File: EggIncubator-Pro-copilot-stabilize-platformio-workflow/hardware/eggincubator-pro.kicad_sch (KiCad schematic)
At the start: 36 parts, among them J1 ESP32 DevKit breakout, J10 ESP32 DevKit 5V / VIN input, J11 BTS7960 motor supply input, J2 SHT31 module, I2C 0x44, J3 DS18B20, 1-Wire, J4 4 optocoupled relay-control o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, J5 BTS7960 module / motor (separ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, J6 Door and turner limit switches, J7 5V buzzer module, Q1 low-side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, J8 Expansion: I2C / ADC sensors, J9 12V DC input, Q1 PN2222A, U1 PC817, U2 PC817, U3 PC817, U4 PC817, U9 12V to 5V buck module

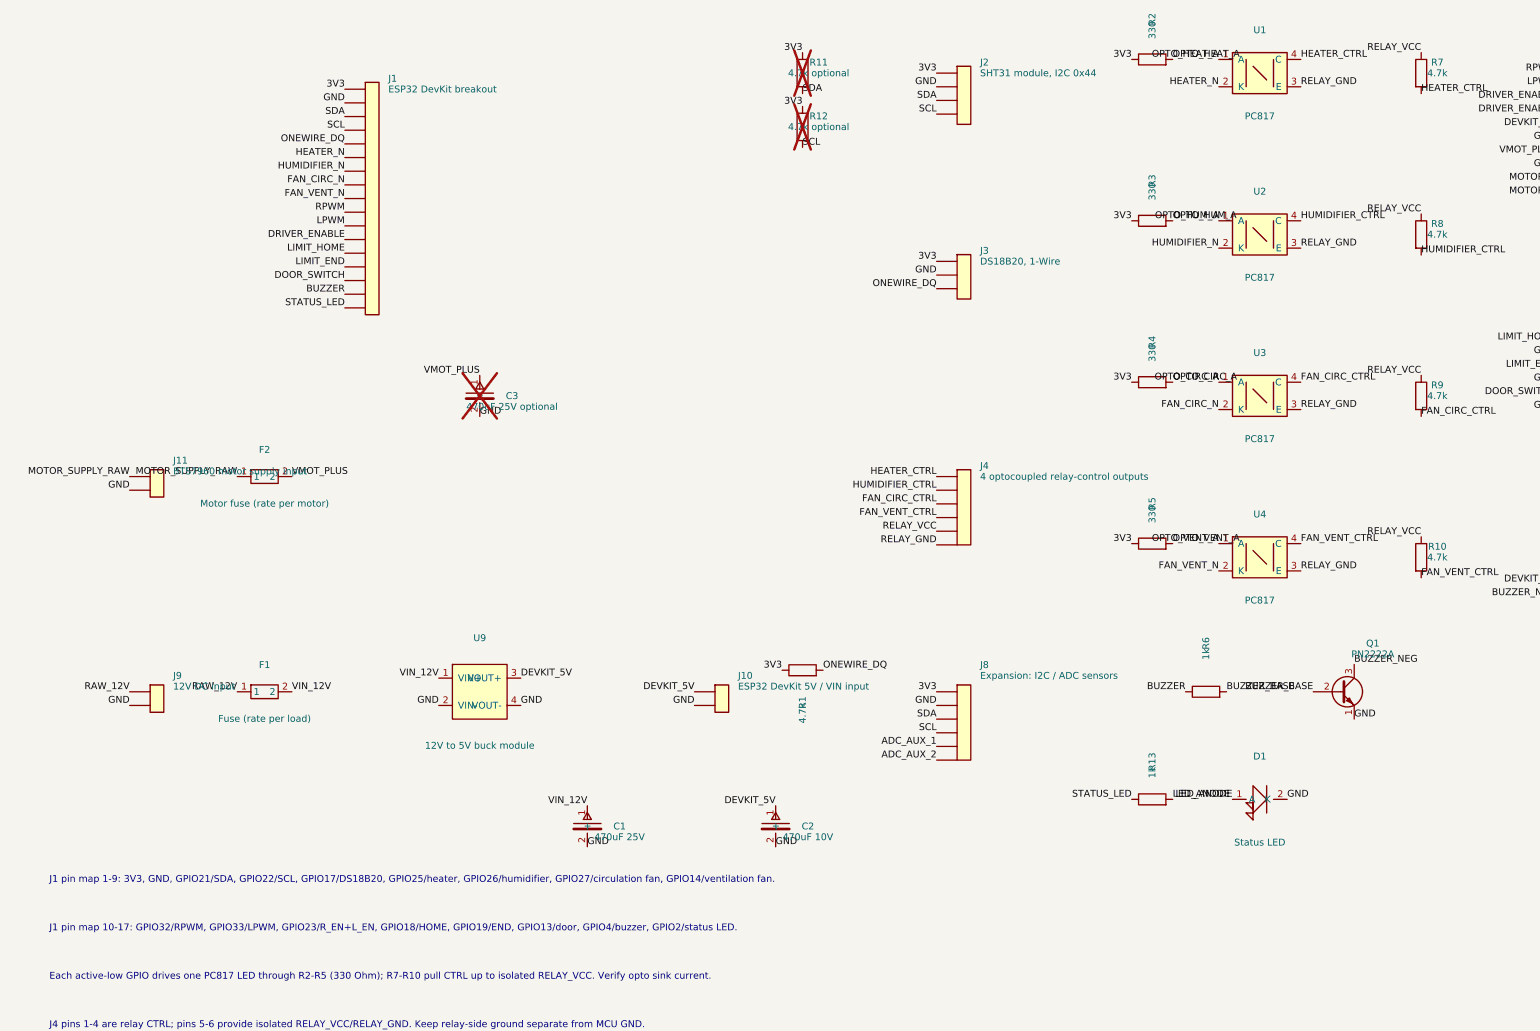
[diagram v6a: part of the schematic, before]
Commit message: Show ESP32 DevKit in KiCad schematic
Co-authored-by: tomnyle <175001228+tomnyle@users.noreply.github.com>
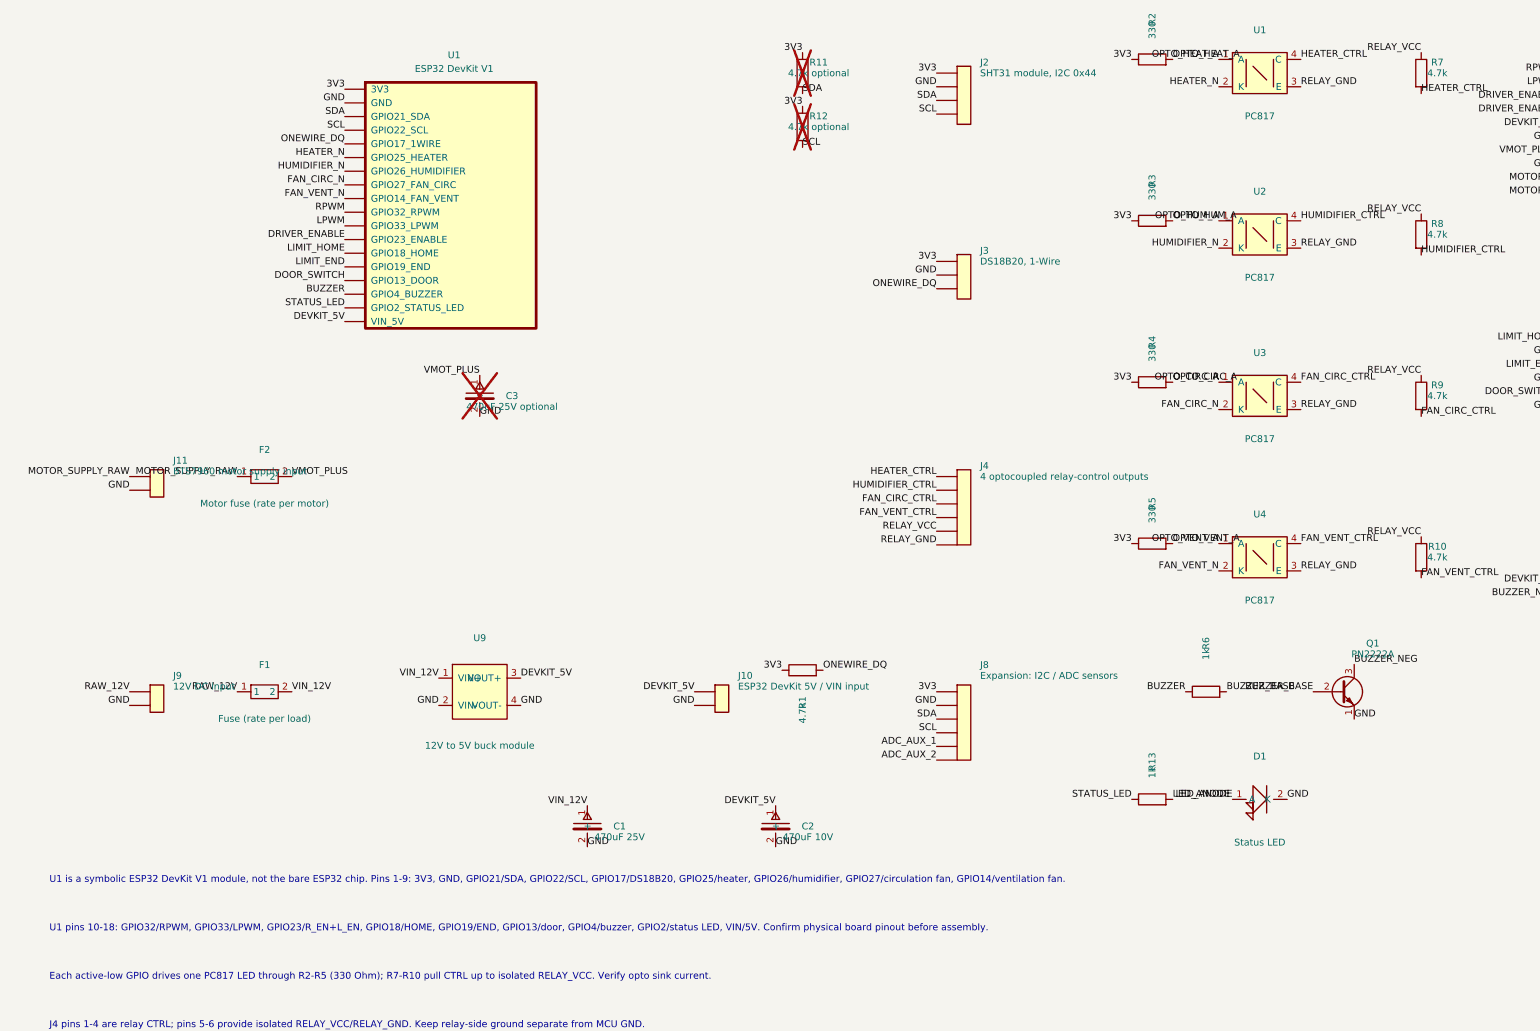
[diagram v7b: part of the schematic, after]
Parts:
- removed J1: ESP32 DevKit breakout, symbol Connector_Generic:Conn_01x17
- added U1: ESP32 DevKit V1, symbol EggIncubator:ESP32_DevKit_V1
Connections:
- net 3V3: now also U1.1 (3V3)
- net BUZZER: now also U1.16 (GPIO4_BUZZER)
- net DEVKIT_5V: now also U1.18 (VIN_5V)
- net DOOR_SWITCH: now also U1.15 (GPIO13_DOOR)
- net DRIVER_ENABLE: now also U1.12 (GPIO23_ENABLE)
- net FAN_CIRC_N: now also U1.8 (GPIO27_FAN_CIRC)
- net FAN_VENT_N: now also U1.9 (GPIO14_FAN_VENT)
- net GND: now also U1.2 (GND)
- net HEATER_N: now also U1.6 (GPIO25_HEATER)
- net HUMIDIFIER_N: now also U1.7 (GPIO26_HUMIDIFIER)
- net LIMIT_END: now also U1.14 (GPIO19_END)
- net LIMIT_HOME: now also U1.13 (GPIO18_HOME)
- net LPWM: now also U1.11 (GPIO33_LPWM)
- net ONEWIRE_DQ: now also U1.5 (GPIO17_1WIRE)
- net RPWM: now also U1.10 (GPIO32_RPWM)
- net SCL: now also U1.4 (GPIO22_SCL)
- net SDA: now also U1.3 (GPIO21_SDA)
- net STATUS_LED: now also U1.17 (GPIO2_STATUS_LED)
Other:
- note added: "U1 is a symbolic ESP32 DevKit V1 module, not the bare ESP32 chip. Pins 1-9: 3V3, GND, GPIO21/SDA, GPIO22/SCL, GPIO17/DS18B20, GPIO25/heater, GPIO26/humidifier, GPIO27/circulation fan, GPIO14/ventilation fan."
- note added: "U1 pins 10-18: GPIO32/RPWM, GPIO33/LPWM, GPIO23/R_EN+L_EN, GPIO18/HOME, GPIO19/END, GPIO13/door, GPIO4/buzzer, GPIO2/status LED, VIN/5V. Confirm physical board pinout before assembly."
- note removed: "J1 pin map 1-9: 3V3, GND, GPIO21/SDA, GPIO22/SCL, GPIO17/DS18B20, GPIO25/heater, GPIO26/humidifier, GPIO27/circulation fan, GPIO14/ventilation fan."
- note removed: "J1 pin map 10-17: GPIO32/RPWM, GPIO33/LPWM, GPIO23/R_EN+L_EN, GPIO18/HOME, GPIO19/END, GPIO13/door, GPIO4/buzzer, GPIO2/status LED."
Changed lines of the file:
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@@
     (comment 2 "Not a mains wiring or PCB fabrication drawing.")
   )
-  (symbol (lib_id "Connector_Generic:Conn_01x17") (at 105 58 0) (unit 1) (in_bom yes) (on_board yes) (dnp no)
-    (property "Reference" "J1" (at 108 56 0) (effects (font (size 1.27 1.27)) (justify left)))
-    (property "Value" "ESP32 DevKit breakout" (at 108 58 0) (effects (font (size 1.27 1.27)) (justify left)))
+  (symbol (lib_id "EggIncubator:ESP32_DevKit_V1") (at 105 58 0) (unit 1) (in_bom yes) (on_board yes) (dnp no)
+    (property "Reference" "U1" (at 120.24 51.65 0) (effects (font (size 1.27 1.27)) (justify center)))
+    (property "Value" "ESP32 DevKit V1" (at 120.24 54.19 0) (effects (font (size 1.27 1.27)) (justify center)))
     (property "Footprint" "" (at 105 58 0) (effects (font (size 1.27 1.27)) hide))
     (property "Datasheet" "~" (at 105 58 0) (effects (font (size 1.27 1.27)) hide))
-    (pin "1") (pin "2") (pin "3") (pin "4") (pin "5") (pin "6") (pin "7") (pin "8") (pin "9") (pin "10") (pin "11") (pin "12") (pin "13") (pin "14") (pin "15") (pin "16") (pin "17")
-    (instances (project "EggIncubator-Pro" (path "/60845d38-2cd0-4dd2-9a8c-c6c7c694e4e9/a165544d-56cd-43db-9b9d-925791539cc0" (reference "J1") (unit 1))))
+    (pin "1")
+    (pin "2")
+    (pin "3")
+    (pin "4")
+    (pin "5")
+    (pin "6")
+    (pin "7")
+    (pin "8")
+    (pin "9")
+    (pin "10")
+    (pin "11")
+    (pin "12")
+    (pin "13")
+    (pin "14")
+    (pin "15")
+    (pin "16")
+    (pin "17")
+    (pin "18")
+    (instances (project "EggIncubator-Pro" (path "/60845d38-2cd0-4dd2-9a8c-c6c7c694e4e9/00000000-0000-4000-8000-000000000173" (reference "U1") (unit 1))))
   )
   (symbol (lib_id "Connector_Generic:Conn_01x04") (at 215 55 0) (unit 1) (in_bom yes) (on_board yes) (dnp no)
@@
   (label "BUZZER" (at 99.92 96.10 180) (fields_autoplaced) (effects (font (size 1.27 1.27)) (justify right bottom)))
   (label "STATUS_LED" (at 99.92 98.64 180) (fields_autoplaced) (effects (font (size 1.27 1.27)) (justify right bottom)))
+  (label "DEVKIT_5V" (at 99.92 101.18 180) (fields_autoplaced) (effects (font (size 1.27 1.27)) (justify right bottom)))
   (label "3V3" (at 209.92 55 180) (fields_autoplaced) (effects (font (size 1.27 1.27)) (justify right bottom)))
   (label "GND" (at 209.92 57.54 180) (fields_autoplaced) (effects (font (size 1.27 1.27)) (justify right bottom)))
@@
   (label "VMOT_PLUS" (at 125 111.19 180) (fields_autoplaced) (effects (font (size 1.27 1.27)) (justify right bottom)))
   (label "GND" (at 125 118.81 0) (fields_autoplaced) (effects (font (size 1.27 1.27)) (justify left bottom)))
-  (text "J1 pin map 1-9: 3V3, GND, GPIO21/SDA, GPIO22/SCL, GPIO17/DS18B20, GPIO25/heater, GPIO26/humidifier, GPIO27/circulation fan, GPIO14/ventilation fan." (at 45 205 0) (effects (font (size 1.27 1.27)) (justify left)))
-  (text "J1 pin map 10-17: GPIO32/RPWM, GPIO33/LPWM, GPIO23/R_EN+L_EN, GPIO18/HOME, GPIO19/END, GPIO13/door, GPIO4/buzzer, GPIO2/status LED." (at 45 214 0) (effects (font (size 1.27 1.27)) (justify left)))
+  (text "U1 is a symbolic ESP32 DevKit V1 module, not the bare ESP32 chip. Pins 1-9: 3V3, GND, GPIO21/SDA, GPIO22/SCL, GPIO17/DS18B20, GPIO25/heater, GPIO26/humidifier, GPIO27/circulation fan, GPIO14/ventilation fan." (at 45 205 0) (effects (font (size 1.27 1.27)) (justify left)))
+  (text "U1 pins 10-18: GPIO32/RPWM, GPIO33/LPWM, GPIO23/R_EN+L_EN, GPIO18/HOME, GPIO19/END, GPIO13/door, GPIO4/buzzer, GPIO2/status LED, VIN/5V. Confirm physical board pinout before assembly." (at 45 214 0) (effects (font (size 1.27 1.27)) (justify left)))
   (text "Each active-low GPIO drives one PC817 LED through R2-R5 (330 Ohm); R7-R10 pull CTRL up to isolated RELAY_VCC. Verify opto sink current." (at 45 223 0) (effects (font (size 1.27 1.27)) (justify left)))
   (text "J4 pins 1-4 are relay CTRL; pins 5-6 provide isolated RELAY_VCC/RELAY_GND. Keep relay-side ground separate from MCU GND." (at 45 232 0) (effects (font (size 1.27 1.27)) (justify left)))

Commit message: Fix ESP32 reference and relay supply notes
Co-authored-by: tomnyle <175001228+tomnyle@users.noreply.github.com>
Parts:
- renumbered U1 to U5
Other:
- note added: "U5 is a symbolic ESP32 DevKit V1 module, not the bare ESP32 chip. Pins 1-9: 3V3, GND, GPIO21/SDA, GPIO22/SCL, GPIO17/DS18B20, GPIO25/heater, GPIO26/humidifier, GPIO27/circulation fan, GPIO14/ventilation fan."
- note added: "U5 pins 10-18: GPIO32/RPWM, GPIO33/LPWM, GPIO23/R_EN+L_EN, GPIO18/HOME, GPIO19/END, GPIO13/door, GPIO4/buzzer, GPIO2/status LED, VIN/5V. Confirm physical board pinout before assembly."
- note removed: "U1 is a symbolic ESP32 DevKit V1 module, not the bare ESP32 chip. Pins 1-9: 3V3, GND, GPIO21/SDA, GPIO22/SCL, GPIO17/DS18B20, GPIO25/heater, GPIO26/humidifier, GPIO27/circulation fan, GPIO14/ventilation fan."
- note removed: "U1 pins 10-18: GPIO32/RPWM, GPIO33/LPWM, GPIO23/R_EN+L_EN, GPIO18/HOME, GPIO19/END, GPIO13/door, GPIO4/buzzer, GPIO2/status LED, VIN/5V. Confirm physical board pinout before assembly."
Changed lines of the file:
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@@
   )
   (symbol (lib_id "EggIncubator:ESP32_DevKit_V1") (at 105 58 0) (unit 1) (in_bom yes) (on_board yes) (dnp no)
-    (property "Reference" "U1" (at 120.24 51.65 0) (effects (font (size 1.27 1.27)) (justify center)))
+    (property "Reference" "U5" (at 120.24 51.65 0) (effects (font (size 1.27 1.27)) (justify center)))
     (property "Value" "ESP32 DevKit V1" (at 120.24 54.19 0) (effects (font (size 1.27 1.27)) (justify center)))
     (property "Footprint" "" (at 105 58 0) (effects (font (size 1.27 1.27)) hide))
@@
     (pin "17")
     (pin "18")
-    (instances (project "EggIncubator-Pro" (path "/60845d38-2cd0-4dd2-9a8c-c6c7c694e4e9/00000000-0000-4000-8000-000000000173" (reference "U1") (unit 1))))
+    (instances (project "EggIncubator-Pro" (path "/60845d38-2cd0-4dd2-9a8c-c6c7c694e4e9/00000000-0000-4000-8000-000000000173" (reference "U5") (unit 1))))
   )
   (symbol (lib_id "Connector_Generic:Conn_01x04") (at 215 55 0) (unit 1) (in_bom yes) (on_board yes) (dnp no)
@@
   (label "VMOT_PLUS" (at 125 111.19 180) (fields_autoplaced) (effects (font (size 1.27 1.27)) (justify right bottom)))
   (label "GND" (at 125 118.81 0) (fields_autoplaced) (effects (font (size 1.27 1.27)) (justify left bottom)))
-  (text "U1 is a symbolic ESP32 DevKit V1 module, not the bare ESP32 chip. Pins 1-9: 3V3, GND, GPIO21/SDA, GPIO22/SCL, GPIO17/DS18B20, GPIO25/heater, GPIO26/humidifier, GPIO27/circulation fan, GPIO14/ventilation fan." (at 45 205 0) (effects (font (size 1.27 1.27)) (justify left)))
-  (text "U1 pins 10-18: GPIO32/RPWM, GPIO33/LPWM, GPIO23/R_EN+L_EN, GPIO18/HOME, GPIO19/END, GPIO13/door, GPIO4/buzzer, GPIO2/status LED, VIN/5V. Confirm physical board pinout before assembly." (at 45 214 0) (effects (font (size 1.27 1.27)) (justify left)))
+  (text "U5 is a symbolic ESP32 DevKit V1 module, not the bare ESP32 chip. Pins 1-9: 3V3, GND, GPIO21/SDA, GPIO22/SCL, GPIO17/DS18B20, GPIO25/heater, GPIO26/humidifier, GPIO27/circulation fan, GPIO14/ventilation fan." (at 45 205 0) (effects (font (size 1.27 1.27)) (justify left)))
+  (text "U5 pins 10-18: GPIO32/RPWM, GPIO33/LPWM, GPIO23/R_EN+L_EN, GPIO18/HOME, GPIO19/END, GPIO13/door, GPIO4/buzzer, GPIO2/status LED, VIN/5V. Confirm physical board pinout before assembly." (at 45 214 0) (effects (font (size 1.27 1.27)) (justify left)))
   (text "Each active-low GPIO drives one PC817 LED through R2-R5 (330 Ohm); R7-R10 pull CTRL up to isolated RELAY_VCC. Verify opto sink current." (at 45 223 0) (effects (font (size 1.27 1.27)) (justify left)))
   (text "J4 pins 1-4 are relay CTRL; pins 5-6 provide isolated RELAY_VCC/RELAY_GND. Keep relay-side ground separate from MCU GND." (at 45 232 0) (effects (font (size 1.27 1.27)) (justify left)))
